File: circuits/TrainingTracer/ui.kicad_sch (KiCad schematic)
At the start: 6 parts, among them J3 OLED_DSP, SW2 SW1, SW3 SW2

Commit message: 回路完成
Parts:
- removed JP3: ON_BUZZER, symbol Jumper:SolderJumper_2_Open
- added J20: SDL, Connector_PinHeader_1.00mm:PinHeader_1x01_P1.00mm_Vertical, symbol Connector_Generic:Conn_01x01
- added J21: SCL, Connector_PinHeader_1.00mm:PinHeader_1x01_P1.00mm_Vertical, symbol Connector_Generic:Conn_01x01
- BZ1: footprint (none) -> Buzzer_Beeper:Buzzer_12x9.5RM7.6
- C5: value C_Small -> 1uF; footprint (none) -> Capacitor_THT:C_Disc_D5.0mm_W2.5mm_P5.00mm
- J13: renamed from J3; footprint (none) -> Connector_JST:JST_ZH_B4B-ZR_1x04_P1.50mm_Vertical
- SW2, SW3: footprint (none) -> Button_Switch_THT:SW_PUSH_6mm_H7.3mm
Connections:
- net SCL: now also J21.1 (Pin_1)
- net SDA: now also J20.1 (Pin_1)
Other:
- moved on the sheet: C5

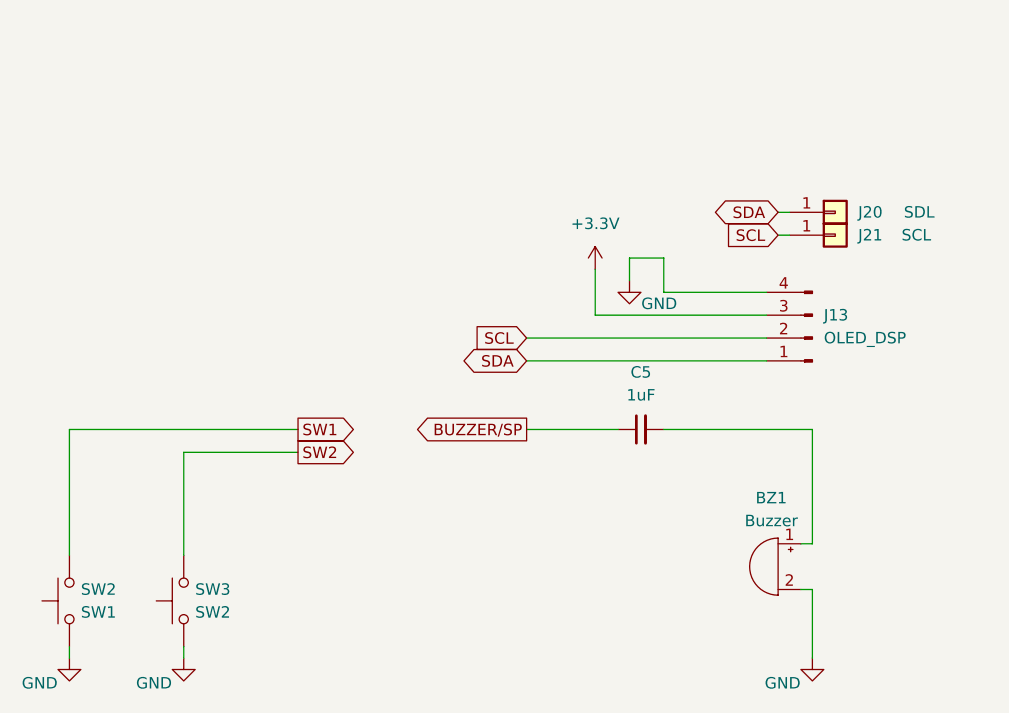
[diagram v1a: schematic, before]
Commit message: PCBのPDF出力
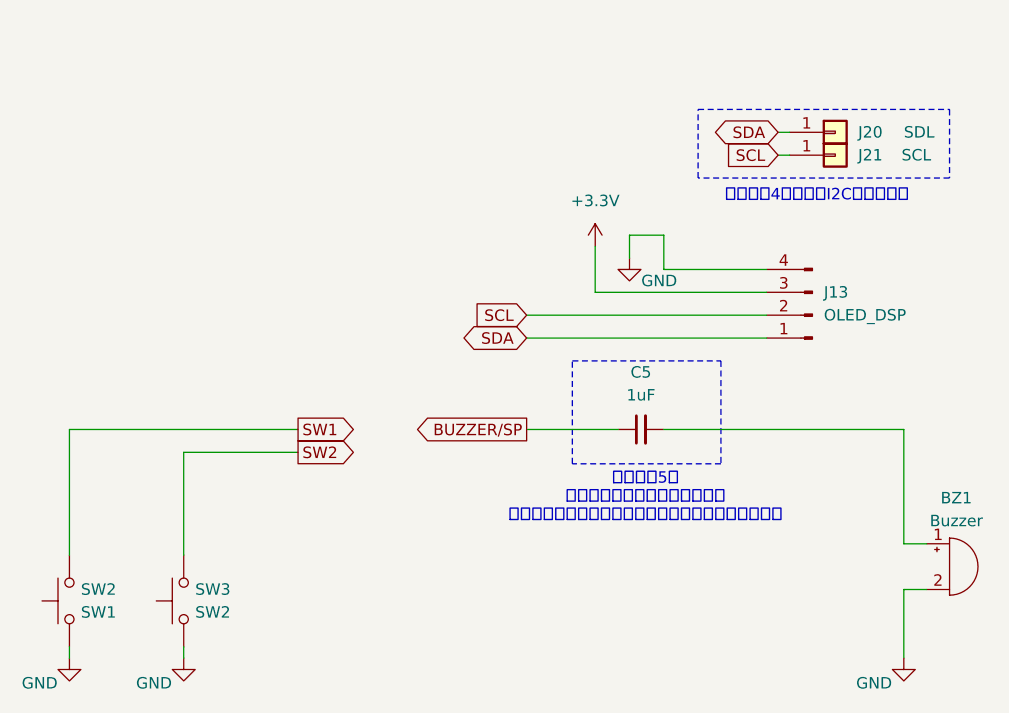
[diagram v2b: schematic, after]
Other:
- note added: "改造箇所4：汎用のI2Cピンアウト"
- note added: "改造箇所5： 圧電素子時の場合はコンデンサ 自励ブザーの場合はコンデンサをジャンパでショート"
- moved on the sheet: BZ1, J13, J20, J21

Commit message: 改造箇所の漏れを追加 (+その他)
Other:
- note added: "改造箇所5：OLEDディスプレイ用のコネクタ追加"
- note added: "改造箇所6： 圧電素子時の場合はコンデンサ 自励ブザーの場合はコンデンサをジャンパでショート"
- note removed: "改造箇所5： 圧電素子時の場合はコンデンサ 自励ブザーの場合はコンデンサをジャンパでショート"
- moved on the sheet: J13, J20, J21
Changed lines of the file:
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@@
 	(paper "A4")
 	(rectangle
-		(start 133.35 53.34)
-		(end 161.29 60.96)
+		(start 97.79 55.88)
+		(end 152.4 76.2)
+		(stroke
+			(width 0)
+			(type dash_dot)
+		)
+		(fill
+			(type none)
+		)
+	)
+	(rectangle
+		(start 124.46 43.18)
+		(end 152.4 50.8)
 		(stroke
 			(width 0)
@@
 		)
 	)
-	(text "改造箇所5：\n圧電素子時の場合はコンデンサ\n自励ブザーの場合はコンデンサをジャンパでショート"
+	(text "改造箇所6：\n圧電素子時の場合はコンデンサ\n自励ブザーの場合はコンデンサをジャンパでショート"
 		(exclude_from_sim no)
 		(at 127.508 96.52 0)
@@
 		)
 	)
-	(text "改造箇所4：汎用のI2Cピンアウト"
-		(exclude_from_sim no)
-		(at 146.558 62.992 0)
+	(text "改造箇所5：OLEDディスプレイ用のコネクタ追加"
+		(exclude_from_sim no)
+		(at 140.97 78.486 0)
 		(effects
 			(font
@@
 		)
 	)
+	(text "改造箇所4：汎用のI2Cピンアウト"
+		(exclude_from_sim no)
+		(at 137.668 52.832 0)
+		(effects
+			(font
+				(size 1.27 1.27)
+			)
+		)
+	)
 	(wire
 		(pts
@@
 	(wire
 		(pts
-			(xy 142.24 58.42) (xy 143.51 58.42)
-		)
-		(stroke
-			(width 0)
-			(type default)
-		)
-	)
-	(wire
-		(pts
-			(xy 129.54 67.31) (xy 129.54 71.12)
-		)
-		(stroke
-			(width 0)
-			(type default)
-		)
-	)
-	(wire
-		(pts
-			(xy 129.54 71.12) (xy 140.97 71.12)
-		)
-		(stroke
-			(width 0)
-			(type default)
-		)
-	)
-	(wire
-		(pts
-			(xy 125.73 69.85) (xy 125.73 67.31)
+			(xy 133.35 48.26) (xy 134.62 48.26)
+		)
+		(stroke
+			(width 0)
+			(type default)
+		)
+	)
+	(wire
+		(pts
+			(xy 123.19 60.96) (xy 123.19 64.77)
+		)
+		(stroke
+			(width 0)
+			(type default)
+		)
+	)
+	(wire
+		(pts
+			(xy 123.19 64.77) (xy 134.62 64.77)
+		)
+		(stroke
+			(width 0)
+			(type default)
+		)
+	)
+	(wire
+		(pts
+			(xy 119.38 63.5) (xy 119.38 60.96)
 		)
 		(stroke
@@
 	(wire
 		(pts
-			(xy 142.24 55.88) (xy 143.51 55.88)
-		)
-		(stroke
-			(width 0)
-			(type default)
-		)
-	)
-	(wire
-		(pts
-			(xy 114.3 76.2) (xy 140.97 76.2)
+			(xy 133.35 45.72) (xy 134.62 45.72)
+		)
+		(stroke
+			(width 0)
+			(type default)
+		)
+	)
+	(wire
+		(pts
+			(xy 107.95 69.85) (xy 134.62 69.85)
 		)
 		(stroke
@@
 	(wire
 		(pts
-			(xy 121.92 73.66) (xy 140.97 73.66)
+			(xy 115.57 67.31) (xy 134.62 67.31)
 		)
 		(stroke
@@
 	(wire
 		(pts
-			(xy 125.73 67.31) (xy 129.54 67.31)
+			(xy 119.38 60.96) (xy 123.19 60.96)
 		)
 		(stroke
@@
 	(wire
 		(pts
-			(xy 114.3 78.74) (xy 140.97 78.74)
+			(xy 107.95 72.39) (xy 134.62 72.39)
 		)
 		(stroke
@@
 	(wire
 		(pts
-			(xy 121.92 68.58) (xy 121.92 73.66)
+			(xy 115.57 62.23) (xy 115.57 67.31)
 		)
 		(stroke
@@
 	(global_label "SCL"
 		(shape input)
-		(at 114.3 76.2 180)
+		(at 107.95 69.85 180)
 		(fields_autoplaced yes)
 		(effects
@@
 		)
 		(property "Intersheetrefs" "${INTERSHEET_REFS}"
-			(at 107.8072 76.2 0)
+			(at 101.4572 69.85 0)
 			(effects
 				(font
@@
 	(global_label "SDA"
 		(shape bidirectional)
-		(at 114.3 78.74 180)
+		(at 107.95 72.39 180)
 		(fields_autoplaced yes)
 		(effects
@@
 		)
 		(property "Intersheetrefs" "${INTERSHEET_REFS}"
-			(at 106.6354 78.74 0)
+			(at 100.2854 72.39 0)
 			(effects
 				(font
@@
 	(global_label "SCL"
 		(shape input)
-		(at 142.24 58.42 180)
+		(at 133.35 48.26 180)
 		(fields_autoplaced yes)
 		(effects
@@
 		)
 		(property "Intersheetrefs" "${INTERSHEET_REFS}"
-			(at 135.7472 58.42 0)
+			(at 126.8572 48.26 0)
 			(effects
 				(font
@@
 	(global_label "SDA"
 		(shape bidirectional)
-		(at 142.24 55.88 180)
+		(at 133.35 45.72 180)
 		(fields_autoplaced yes)
 		(effects
@@
 		)
 		(property "Intersheetrefs" "${INTERSHEET_REFS}"
-			(at 134.5754 55.88 0)
+			(at 125.6854 45.72 0)
 			(effects
 				(font
@@
 	(symbol
 		(lib_id "Connector_Generic:Conn_01x01")
-		(at 148.59 55.88 0)
+		(at 139.7 45.72 0)
 		(unit 1)
 		(exclude_from_sim no)
@@
 		(dnp no)
 		(property "Reference" "J20"
-			(at 151.13 55.88 0)
+			(at 142.24 45.72 0)
 			(effects
 				(font
@@
 		)
 		(property "Value" "SDL"
-			(at 156.21 55.88 0)
+			(at 147.32 45.72 0)
 			(effects
 				(font
@@
 		)
 		(property "Footprint" "Connector_PinHeader_1.00mm:PinHeader_1x01_P1.00mm_Vertical"
-			(at 148.59 55.88 0)
+			(at 139.7 45.72 0)
 			(effects
 				(font
@@
 		)
 		(property "Datasheet" "~"
-			(at 148.59 55.88 0)
+			(at 139.7 45.72 0)
 			(effects
 				(font
@@
 		)
 		(property "Description" "Generic connector, single row, 01x01, script generated (kicad-library-utils/schlib/autogen/connector/)"
-			(at 148.59 55.88 0)
+			(at 139.7 45.72 0)
 			(effects
 				(font
@@
 	(symbol
 		(lib_id "Connector_Generic:Conn_01x01")
-		(at 148.59 58.42 0)
+		(at 139.7 48.26 0)
 		(unit 1)
 		(exclude_from_sim no)
@@
 		(dnp no)
 		(property "Reference" "J21"
-			(at 151.13 58.42 0)
+			(at 142.24 48.26 0)
 			(effects
 				(font
@@
 		)
 		(property "Value" "SCL"
-			(at 155.956 58.42 0)
+			(at 147.066 48.26 0)
 			(effects
 				(font
@@
 		)
 		(property "Footprint" "Connector_PinHeader_1.00mm:PinHeader_1x01_P1.00mm_Vertical"
-			(at 148.59 58.42 0)
+			(at 139.7 48.26 0)
 			(effects
 				(font
@@
 		)
 		(property "Datasheet" "~"
-			(at 148.59 58.42 0)
+			(at 139.7 48.26 0)
 			(effects
 				(font
@@
 		)
 		(property "Description" "Generic connector, single row, 01x01, script generated (kicad-library-utils/schlib/autogen/connector/)"
-			(at 148.59 58.42 0)
+			(at 139.7 48.26 0)
 			(effects
 				(font
@@
 	(symbol
 		(lib_id "power:GND")
-		(at 125.73 69.85 0)
+		(at 119.38 63.5 0)
 		(unit 1)
 		(exclude_from_sim no)
@@
 		(dnp no)
 		(property "Reference" "#PWR056"
-			(at 125.73 76.2 0)
+			(at 119.38 69.85 0)
 			(effects
 				(font
@@
 		)
 		(property "Value" "GND"
-			(at 129.032 72.39 0)
+			(at 122.682 66.04 0)
 			(effects
 				(font
@@
 		)
 		(property "Footprint" ""
-			(at 125.73 69.85 0)
+			(at 119.38 63.5 0)
 			(effects
 				(font
@@
 		)
 		(property "Datasheet" ""
-			(at 125.73 69.85 0)
+			(at 119.38 63.5 0)
 			(effects
 				(font
@@
 		)
 		(property "Description" "Power symbol creates a global label with name \"GND\" , ground"
-			(at 125.73 69.85 0)
+			(at 119.38 63.5 0)
 			(effects
 				(font
@@
 	(symbol
 		(lib_id "power:+3.3V")
-		(at 121.92 68.58 0)
+		(at 115.57 62.23 0)
 		(unit 1)
 		(exclude_from_sim no)
@@
 		(fields_autoplaced yes)
 		(property "Reference" "#PWR055"
-			(at 121.92 72.39 0)
+			(at 115.57 66.04 0)
 			(effects
 				(font
@@
 		)
 		(property "Value" "+3.3V"
-			(at 121.92 63.5 0)
+			(at 115.57 57.15 0)
 			(effects
 				(font
@@
 		)
 		(property "Footprint" ""
-			(at 121.92 68.58 0)
+			(at 115.57 62.23 0)
 			(effects
 				(font
@@
 		)
 		(property "Datasheet" ""
-			(at 121.92 68.58 0)
+			(at 115.57 62.23 0)
 			(effects
 				(font
@@
 		)
 		(property "Description" "Power symbol creates a global label with name \"+3.3V\""
-			(at 121.92 68.58 0)
+			(at 115.57 62.23 0)
 			(effects
 				(font
@@
 	(symbol
 		(lib_id "Connector:Conn_01x04_Pin")
-		(at 146.05 76.2 180)
+		(at 139.7 69.85 180)
 		(unit 1)
 		(exclude_from_sim no)
@@
 		(fields_autoplaced yes)
 		(property "Reference" "J13"
-			(at 147.32 73.6599 0)
+			(at 140.97 67.3099 0)
 			(effects
 				(font
@@
 		)
 		(property "Value" "OLED_DSP"
-			(at 147.32 76.1999 0)
+			(at 140.97 69.8499 0)
 			(effects
 				(font
@@
 		)
 		(property "Footprint" "Connector_JST:JST_ZH_B4B-ZR_1x04_P1.50mm_Vertical"
-			(at 146.05 76.2 0)
+			(at 139.7 69.85 0)
 			(effects
 				(font
@@
 		)
 		(property "Datasheet" "~"
-			(at 146.05 76.2 0)
+			(at 139.7 69.85 0)
 			(effects
 				(font
@@
 		)
 		(property "Description" "Generic connector, single row, 01x04, script generated"
-			(at 146.05 76.2 0)
-			(effects
-				(font
+			(at 139.7 69.85 0)
+			(effects
+				(font
